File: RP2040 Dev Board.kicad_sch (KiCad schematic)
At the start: 9 parts, among them J101 Conn_01x19, J102 Conn_01x19, J103 Conn_01x03

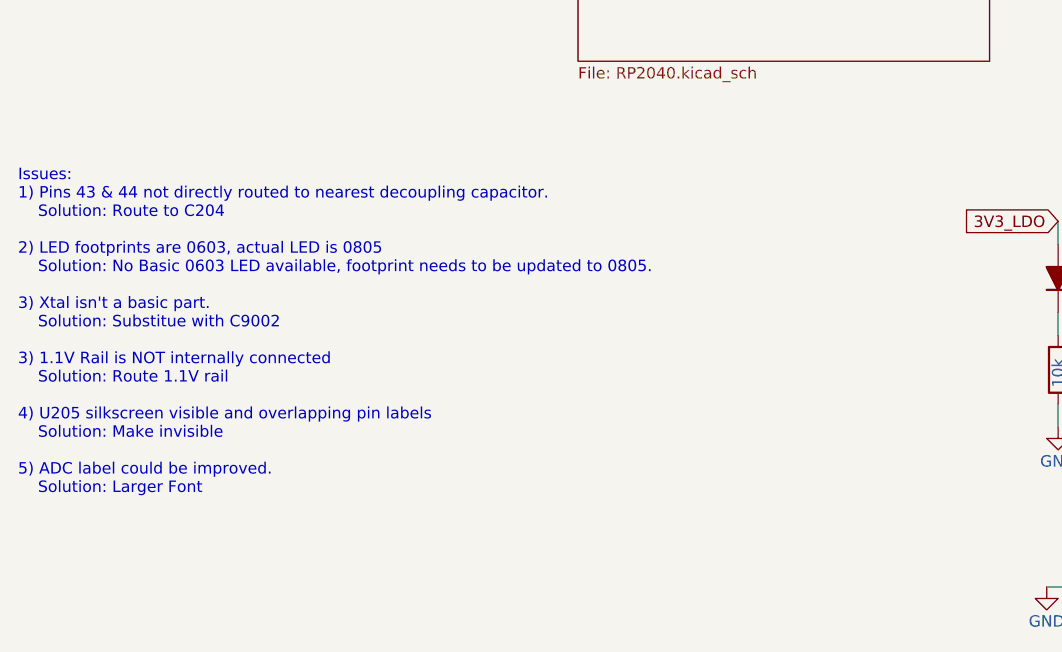
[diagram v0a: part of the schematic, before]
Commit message: Rev 2
Ready to order Rev2:
-Routed missing 1.1V rail
-Swapped LED footprints from 0603 to 0805
-Pins 43 &44 routed to nearest decoupling cap
-Crystal replaced with basic part and created 3D model
-ADC silkscreen improved
-Minor Silkscreen changes
-Generated new gerbers, renders, and PDFs
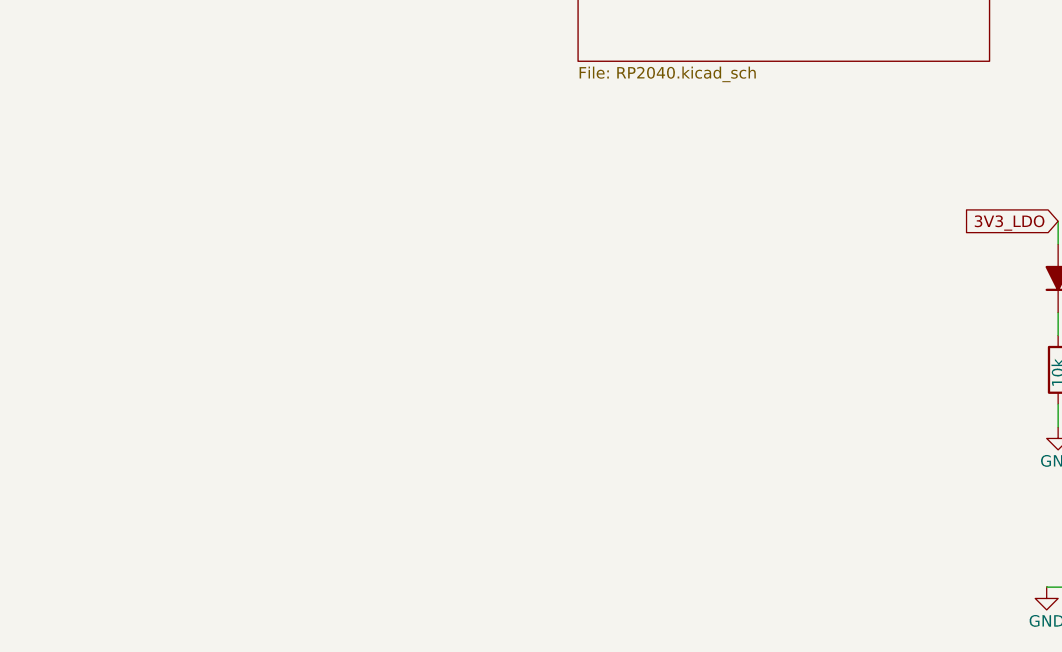
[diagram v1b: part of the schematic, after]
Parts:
- D101, D102: footprint (none) -> LED_SMD:LED_0805_2012Metric
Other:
- note removed: "Issues: 1) Pins 43 & 44 not directly routed to nearest decoupling capacitor. Solution: Route to C204 2) LED footprints are 0603, actual LED is 0805 Solution: No Basic 0603 LED available, footprint needs to be updated to 0805. 3) Xtal isn't a basic part. Solution: Substitue with C9002 3) 1.1V Rail is NOT internally connected Solution: Route 1.1V rail 4) U205 silkscreen visible and overlapping pin 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"
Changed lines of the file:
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@@
   (title_block
     (title "RP2040 Template")
-    (date "2022-03-28")
-    (rev "1")
+    (date "2022-04-24")
+    (rev "2")
     (company "J & R Creative Technologies Inc.")
+    (comment 1 "@RangenMichael")
+    (comment 2 "https://twitter.com/RangenMichael")
+    (comment 3 "MIT License")
+    (comment 4 "https://github.com/mrangen/RP2040-Dev-Board")
   )
   (junction (at 200.66 120.65) (diameter 0) (color 0 0 0 0)
@@
   (wire (pts (xy 189.23 125.73) (xy 190.5 125.73))
     (stroke (width 0) (type default) (color 0 0 0 0))
-  )
-  (text "Issues:\n1) Pins 43 & 44 not directly routed to nearest decoupling capacitor.\n	Solution: Route to C204\n\n2) LED footprints are 0603, actual LED is 0805\n	Solution: No Basic 0603 LED available, footprint needs to be updated to 0805.\n\n3) Xtal isn't a basic part.\n	Solution: Substitue with C9002\n\n3) 1.1V Rail is NOT internally connected\n	Solution: Route 1.1V rail\n\n4) U205 silkscreen visible and overlapping pin labels\n	Solution: Make invisible\n\n5) ADC label could be improved.\n	Solution: Larger Font"
-    (at 20.32 139.7 0)
-    (effects (font (size 1.27 1.27)) (justify left bottom))
   )
   (global_label "GPIO18" (shape tri_state) (at 185.42 85.09 180) (fields_autoplaced)
@@
       (effects (font (size 1.27 1.27)) (justify right))
     )
-    (property "Footprint" "" (id 2) (at 135.89 115.57 0)
+    (property "Footprint" "LED_SMD:LED_0805_2012Metric" (id 2) (at 135.89 115.57 0)
       (effects (font (size 1.27 1.27)) hide)
     )
@@
       (effects (font (size 1.27 1.27)) (justify right))
     )
-    (property "Footprint" "" (id 2) (at 153.67 125.73 0)
+    (property "Footprint" "LED_SMD:LED_0805_2012Metric" (id 2) (at 153.67 125.73 0)
       (effects (font (size 1.27 1.27)) hide)
     )
@@
     )
     (path "/3e7bcc2a-10c2-45cd-9897-4c0007e1c7fc/2a22be26-a817-4ed8-b112-95aa7d11fc7c"
-      (reference "Y201") (unit 1) (value "Crystal_GND24") (footprint "Breadstick Footprints:7V12000018")
-    )
-  )
+      (reference "Y201") (unit 1) (value "Crystal_GND24") (footprint "X322516MLB4SI:OSC_X322516MLB4SI")
+    )
+  )

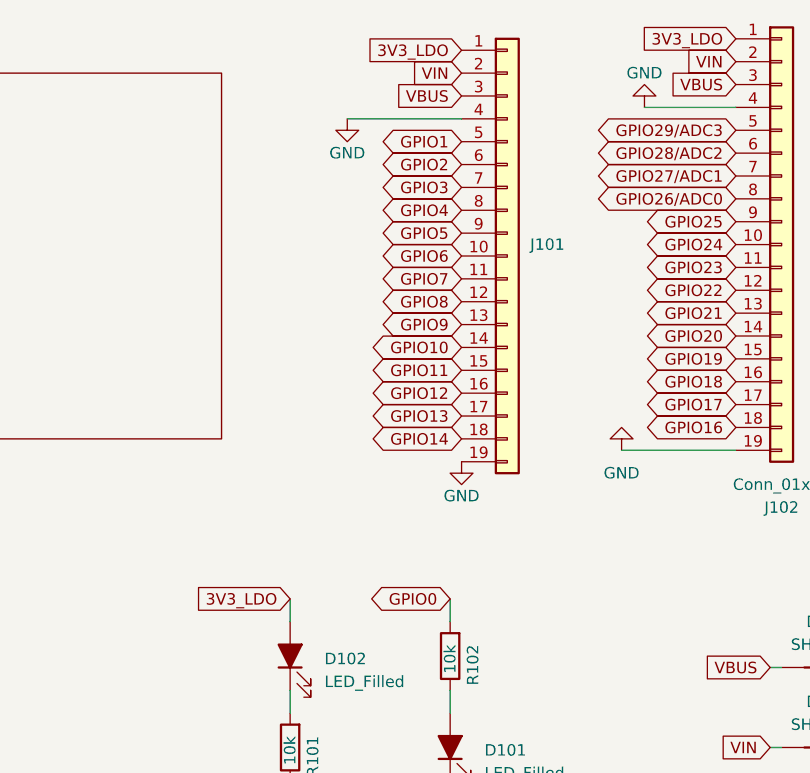
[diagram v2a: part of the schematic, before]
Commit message: Made changes to schematic and PCB
Swapped pin 0 and pin 14.
Added missing trace from regulator to capacitors.
Widened power distribution traces.
Aligned LEDs.
Adjusted Silkscreen.
Updated Revision number to 4
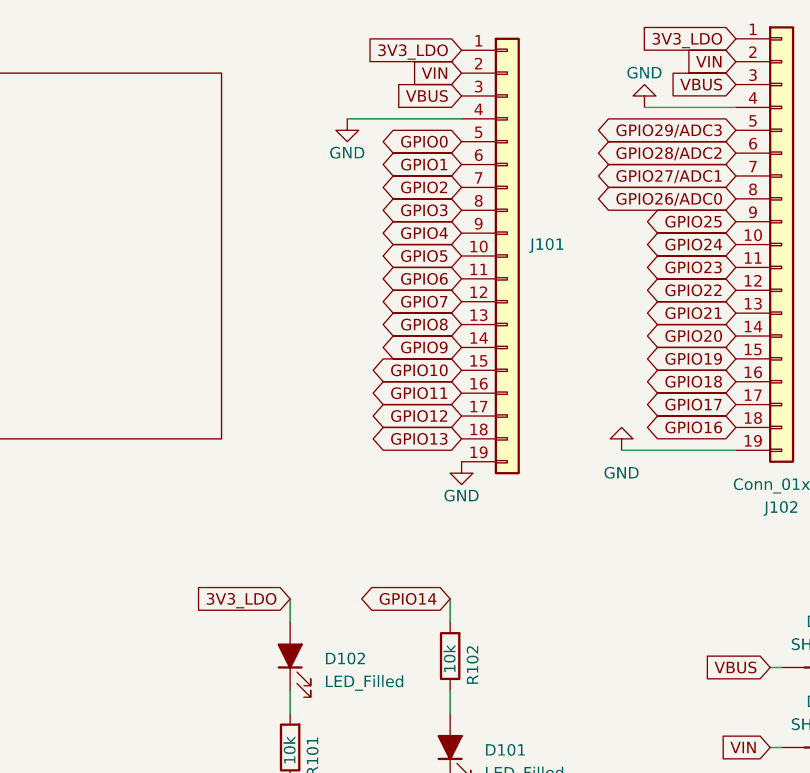
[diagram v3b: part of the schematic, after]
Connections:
- net GPIO0: now also J101.5 (Pin_5); no longer R102.2
- net GPIO1: now also J101.6 (Pin_6); no longer J101.5 (Pin_5)
- net GPIO10: now also J101.15 (Pin_15); no longer J101.14 (Pin_14)
- net GPIO11: now also J101.16 (Pin_16); no longer J101.15 (Pin_15)
- net GPIO12: now also J101.17 (Pin_17); no longer J101.16 (Pin_16)
- net GPIO13: now also J101.18 (Pin_18); no longer J101.17 (Pin_17)
- net GPIO14: now also R102.2; no longer J101.18 (Pin_18)
- net GPIO2: now also J101.7 (Pin_7); no longer J101.6 (Pin_6)
- net GPIO3: now also J101.8 (Pin_8); no longer J101.7 (Pin_7)
- net GPIO4: now also J101.9 (Pin_9); no longer J101.8 (Pin_8)
- net GPIO5: now also J101.10 (Pin_10); no longer J101.9 (Pin_9)
- net GPIO6: now also J101.11 (Pin_11); no longer J101.10 (Pin_10)
- net GPIO7: now also J101.12 (Pin_12); no longer J101.11 (Pin_11)
- net GPIO8: now also J101.13 (Pin_13); no longer J101.12 (Pin_12)
- net GPIO9: now also J101.14 (Pin_14); no longer J101.13 (Pin_13)
